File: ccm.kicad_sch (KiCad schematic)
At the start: 54 parts, among them J1 Conn_01x02_Socket, J10 Conn_01x02_Socket, J2 Conn_01x02_Socket, J3 Conn_01x02_Socket, J4 Conn_01x04_Socket, J5 Conn_01x02_Socket, J6 Conn_01x02_Socket, J7 Conn_01x02_Socket, J8 Conn_01x04_Socket, J9 Conn_01x02_Socket, Q1 IRLZ34N, U1 Teensy4.1, U2 PAM8302AAY, U3 SN65HVD230, U4 SN65HVD230, U5 LM1117DT-5.0

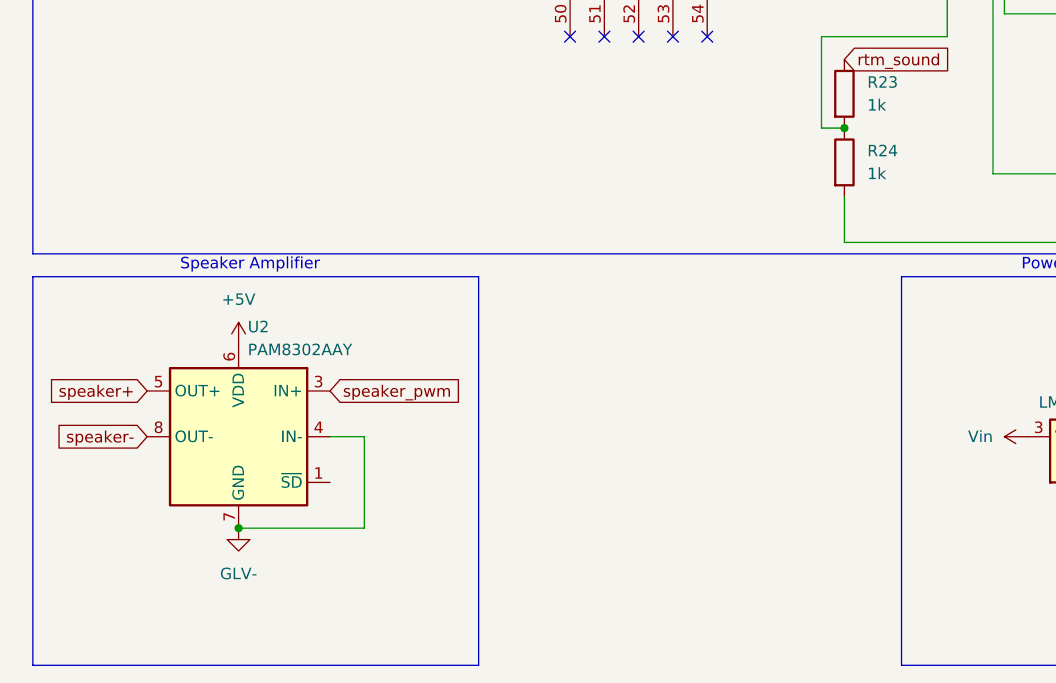
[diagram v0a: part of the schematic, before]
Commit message: added capacitors for amp
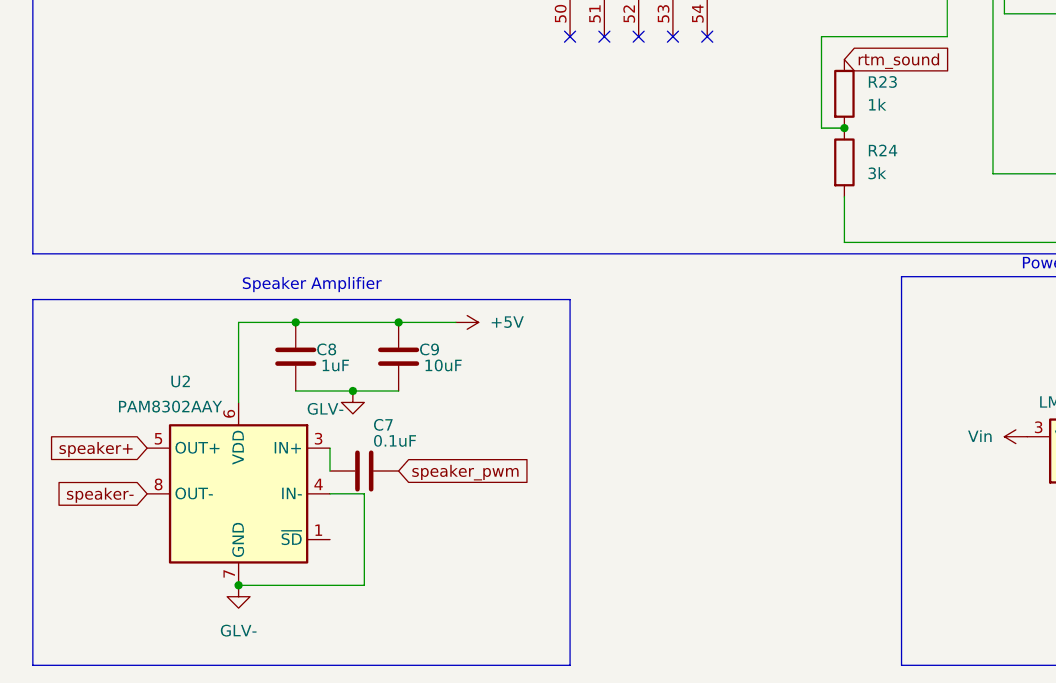
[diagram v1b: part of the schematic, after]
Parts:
- added C7: 0.1uF, Capacitor_SMD:C_0805_2012Metric, symbol Device:C
- added C8: 1uF, Capacitor_SMD:C_0805_2012Metric, symbol Device:C
- added C9: 10uF, Capacitor_SMD:C_0805_2012Metric, symbol Device:C
- R24: value 1k -> 3k
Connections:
- net +5V: now also C8.1, C9.1
- net GLV-: now also C8.2, C9.2
- net speaker_pwm: now also C7.2; no longer U2.3 (IN+)
- new net: C7.1, U2.3 (IN+)
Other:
- moved on the sheet: U2

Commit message: updated to revision schematic
tbd i/o connectors
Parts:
- added D1, D2, D3, D4: 1N5819, Diode_THT:D_DO-41_SOD81_P10.16mm_Horizontal, symbol Diode:1N5819
- added J11, J12, J15, J16: Conn_01x02_Socket, Connector_Molex:Molex_Mini-Fit_Jr_5566-02A2_2x01_P4.20mm_Vertical, symbol Connector:Conn_01x02_Socket
- added J13, J14: Conn_01x04_Socket, Connector_Molex:Molex_Mini-Fit_Jr_5566-04A2_2x02_P4.20mm_Vertical, symbol Connector:Conn_01x04_Socket
- added Q2, Q3, Q4, Q5: IRLZ34N, Package_TO_SOT_THT:TO-220-3_Vertical, symbol Transistor_FET:IRLZ34N
- added R33, R36, R38, R40: 220, symbol Device:R_US
- added R34, R35, R37, R39: 10k, symbol Device:R_US
- added R41, R42, R43, R44: 10k, Resistor_SMD:R_0805_2012Metric, symbol Device:R
- added TH1, TH2, TH3, TH4: Thermistor, symbol Device:Thermistor
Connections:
- net +3.3V: now also R41.2, R42.2, R43.2, R44.2
- net GLV-: now also Q2.3 (S), Q3.3 (S), Q4.3 (S), Q5.3 (S), R34.2, R35.2, R37.2, R39.2, TH1.2, TH2.2, TH3.2, TH4.2
- net lin_pot_1: now also J13.4 (Pin_4), J14.4 (Pin_4)
- net lin_pot_2: now also J13.3 (Pin_3), J14.3 (Pin_3)
- net lin_pot_3: now also J13.2 (Pin_2), J14.2 (Pin_2)
- net lin_pot_4: now also J13.1 (Pin_1), J14.1 (Pin_1)
- net at U1.18 (26_A12_MOSI1): now also R33.2, R34.1
- net at U1.19 (27_A13_SCK1): now also R35.1, R36.2
- net at U1.20 (28_RX7): now also R37.1, R38.2
- net at U1.21 (29_TX7): now also R39.1, R40.2
- net gpio2: now reaches U1.25 (33_MCLK2)
- net gpio3: now reaches U1.26 (34_RX8)
- net flowsensor4: now reaches U1.27 (35_TX8)
- net flowsensor3: now reaches U1.28 (36_CS)
- net flowsensor2: now reaches U1.29 (37_CS)
- net flowsensor1: now reaches U1.30 (38_CS1_IN1)
- net at U1.31 (39_MISO1_OUT1A): now also R44.1, TH4.1
- net at U1.32 (40_A16): now also R43.1, TH3.1
- net at U1.33 (41_A17): now also R42.1, TH2.1
- net at U1.36 (14_A0_TX3_SPDIF_OUT): now also R41.1, TH1.1
- new net: Q2.1 (G), R33.1
- new net: Q5.1 (G), R40.1
- new net: Q3.1 (G), R36.1
- new net: Q4.1 (G), R38.1
- new net +24V: D1.1 (K), D2.1 (K), D3.1 (K), D4.1 (K)
- new net Fan1-: D3.2 (A), Q4.2 (D)
- new net Fan2-: D4.2 (A), Q5.2 (D)
- new net Pump1-: D1.2 (A), Q2.2 (D)
- new net Pump2-: D2.2 (A), Q3.2 (D)
- no-connect marks 45 -> 29
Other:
- moved on the sheet: C1, C2, C3, C4, C5, C6, C7, C8, C9, J1, J10, J2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

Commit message: add i/o connectors
tbd pcb revision
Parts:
- added J17, J18: Conn_01x02_Socket, Connector_Molex:Molex_Mini-Fit_Jr_5566-02A2_2x01_P4.20mm_Vertical, symbol Connector:Conn_01x02_Socket
- added J19: Conn_01x04_Socket, Connector_Molex:Molex_Mini-Fit_Jr_5566-04A2_2x02_P4.20mm_Vertical, symbol Connector:Conn_01x04_Socket
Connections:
- net gpio3 is gone; now on net gpio2: U1.26 (34_RX8)
- net +24V: now also J11.1 (Pin_1), J12.1 (Pin_1), J15.1 (Pin_1), J16.1 (Pin_1)
- net Fan1-: now also J15.2 (Pin_2)
- net Fan2-: now also J16.2 (Pin_2)
- net GLV-: now also J17.2 (Pin_2), J18.2 (Pin_2)
- net Pump1-: now also J11.2 (Pin_2)
- net Pump2-: now also J12.2 (Pin_2)
- net flowsensor1: now also J13.4 (Pin_4)
- net flowsensor2: now also J13.3 (Pin_3)
- net flowsensor3: now also J13.2 (Pin_2)
- net flowsensor4: now also J13.1 (Pin_1)
- net gpio2: now also J18.1 (Pin_1); no longer U1.25 (33_MCLK2)
- net lin_pot_1: no longer J13.4 (Pin_4), J14.4 (Pin_4)
- net lin_pot_2: no longer J13.3 (Pin_3), J14.3 (Pin_3)
- net lin_pot_3: no longer J13.2 (Pin_2), J14.2 (Pin_2)
- net lin_pot_4: no longer J13.1 (Pin_1), J14.1 (Pin_1)
- new net gpio1: J17.1 (Pin_1), U1.25 (33_MCLK2)
- new net thermistor1+: J19.1 (Pin_1)
- new net thermistor1-: J14.1 (Pin_1)
- new net thermistor2+: J19.2 (Pin_2)
- new net thermistor2-: J14.2 (Pin_2)
- new net thermistor3+: J19.3 (Pin_3)
- new net thermistor3-: J14.3 (Pin_3)
- new net thermistor4+: J19.4 (Pin_4)
- new net thermistor4-: J14.4 (Pin_4)
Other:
- note added: "Extra GPIO"
- note added: "Flow Speed Sensors"
- note added: "Pump/Fan Output"
- note added: "Ready To Move Signal"
- note added: "Thermistor"
- note removed: "Board I/O"
- moved on the sheet: C7, C8, C9, J1, J10, J11, J12, J13, J14, J15, J16, J2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

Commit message: ccm schem complete
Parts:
- removed D1, D2, D3, D4: 1N5819, Diode_THT:D_DO-41_SOD81_P10.16mm_Horizontal, symbol Diode:1N5819
- removed J13, J14, J19: Conn_01x04_Socket, Connector_Molex:Molex_Mini-Fit_Jr_5566-04A2_2x02_P4.20mm_Vertical, symbol Connector:Conn_01x04_Socket
- added D1, D2, D3, D4: SS14, Diode_SMD:D_SMA, symbol Diode:SS14
- added J13, J14, J19, J20, J21, J22, J23, J24: Conn_01x02_Socket, Connector_Molex:Molex_Mini-Fit_Jr_5566-02A2_2x01_P4.20mm_Vertical, symbol Connector:Conn_01x02_Socket
- R33, R34, R35, R36, R37, R38, R39, R40: footprint (none) -> Resistor_SMD:R_0805_2012Metric
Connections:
- net +24V: now also D1.1 (K), D2.1 (K), D3.1 (K), D4.1 (K)
- net Fan1-: now also D3.2 (A)
- net Fan2-: now also D4.2 (A)
- net GLV-: now also J13.2 (Pin_2), J19.2 (Pin_2), J20.2 (Pin_2), J21.2 (Pin_2), J22.2 (Pin_2), J23.2 (Pin_2)
- net Pump1-: now also D1.2 (A)
- net Pump2-: now also D2.2 (A)
- net thermistor1+: now also R41.1, TH1.1, U1.36 (14_A0_TX3_SPDIF_OUT), J21.1 (Pin_1)
- net thermistor2+: now also R42.1, TH2.1, U1.33 (41_A17), J19.1 (Pin_1)
- net thermistor3+: now also R43.1, TH3.1, U1.32 (40_A16), J22.1 (Pin_1)
- net thermistor4+: now also J23.1 (Pin_1)
- net Fan2_PWM: now reaches U1.10 (8_TX2_IN1)
- net Fan2_PWM: now also J24.2 (Pin_2)
- net Pump1_PWM: now reaches U1.7 (5_IN2)
- net Pump1_PWM: now also J14.1 (Pin_1)
- net Pump2_PWM: now reaches U1.8 (6_OUT1D)
- net Pump2_PWM: now also J14.2 (Pin_2)
- net Fan1_PWM: now reaches U1.9 (7_RX2_OUT1A)
- net Fan1_PWM: now also J24.1 (Pin_1)
- net flowsensor1: no longer names the net of U1.30 (38_CS1_IN1)
- net flowsensor2: no longer names the net of U1.29 (37_CS)
- net flowsensor3 renamed gpio4
- net gpio4: now also J20.1 (Pin_1)
- net flowsensor4 renamed gpio3
- net gpio3: now also J13.1 (Pin_1)
- no-connect marks 29 -> 25
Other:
- note added: "Extra GPIO Pins"
- note added: "Pump/Fan PWM OUT"
- note removed: "Extra GPIO"
- note removed: "Flow Speed Sensors"
- moved on the sheet: J1, J10, J11, J12, J15, J16, J17, J18, J2, J3, J4, J5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

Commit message: layout v1
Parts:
- removed J14: Conn_01x02_Socket, Connector_Molex:Molex_Mini-Fit_Jr_5566-02A2_2x01_P4.20mm_Vertical, symbol Connector:Conn_01x02_Socket
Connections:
- net GLV-: no longer J19.2 (Pin_2), J21.2 (Pin_2), J22.2 (Pin_2), J23.2 (Pin_2)
- net Pump1_PWM: no longer names the net of U1.7 (5_IN2)
- net Pump2_PWM: no longer names the net of U1.8 (6_OUT1D)
- new net thermistor1-: J21.2 (Pin_2)
- new net thermistor2-: J19.2 (Pin_2)
- new net thermistor3-: J22.2 (Pin_2)
- new net thermistor4-: J23.2 (Pin_2)
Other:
- note added: "Fan PWM OUT"
- note added: "Ready To Move Signal (Redundant)"
- note removed: "Pump/Fan PWM OUT"
- note removed: "Ready To Move Signal"
- moved on the sheet: D1, D2, D3, D4, J24

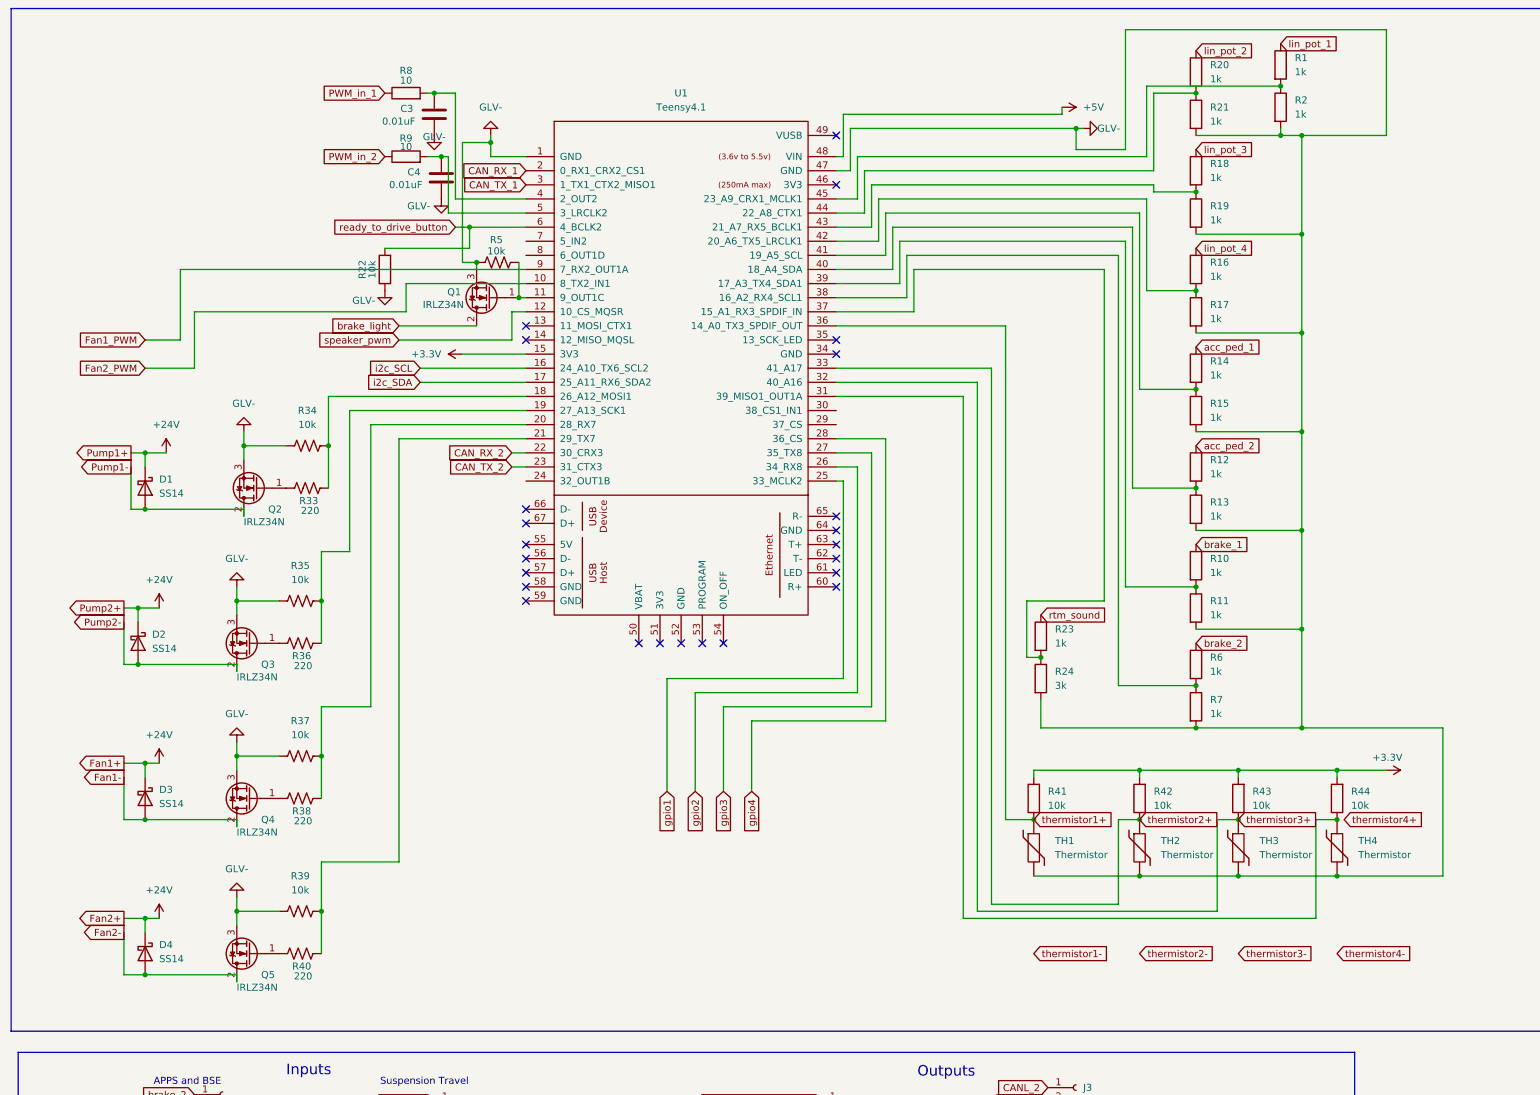
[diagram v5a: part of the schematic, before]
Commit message: add npn transistor level shifter for fan pwm
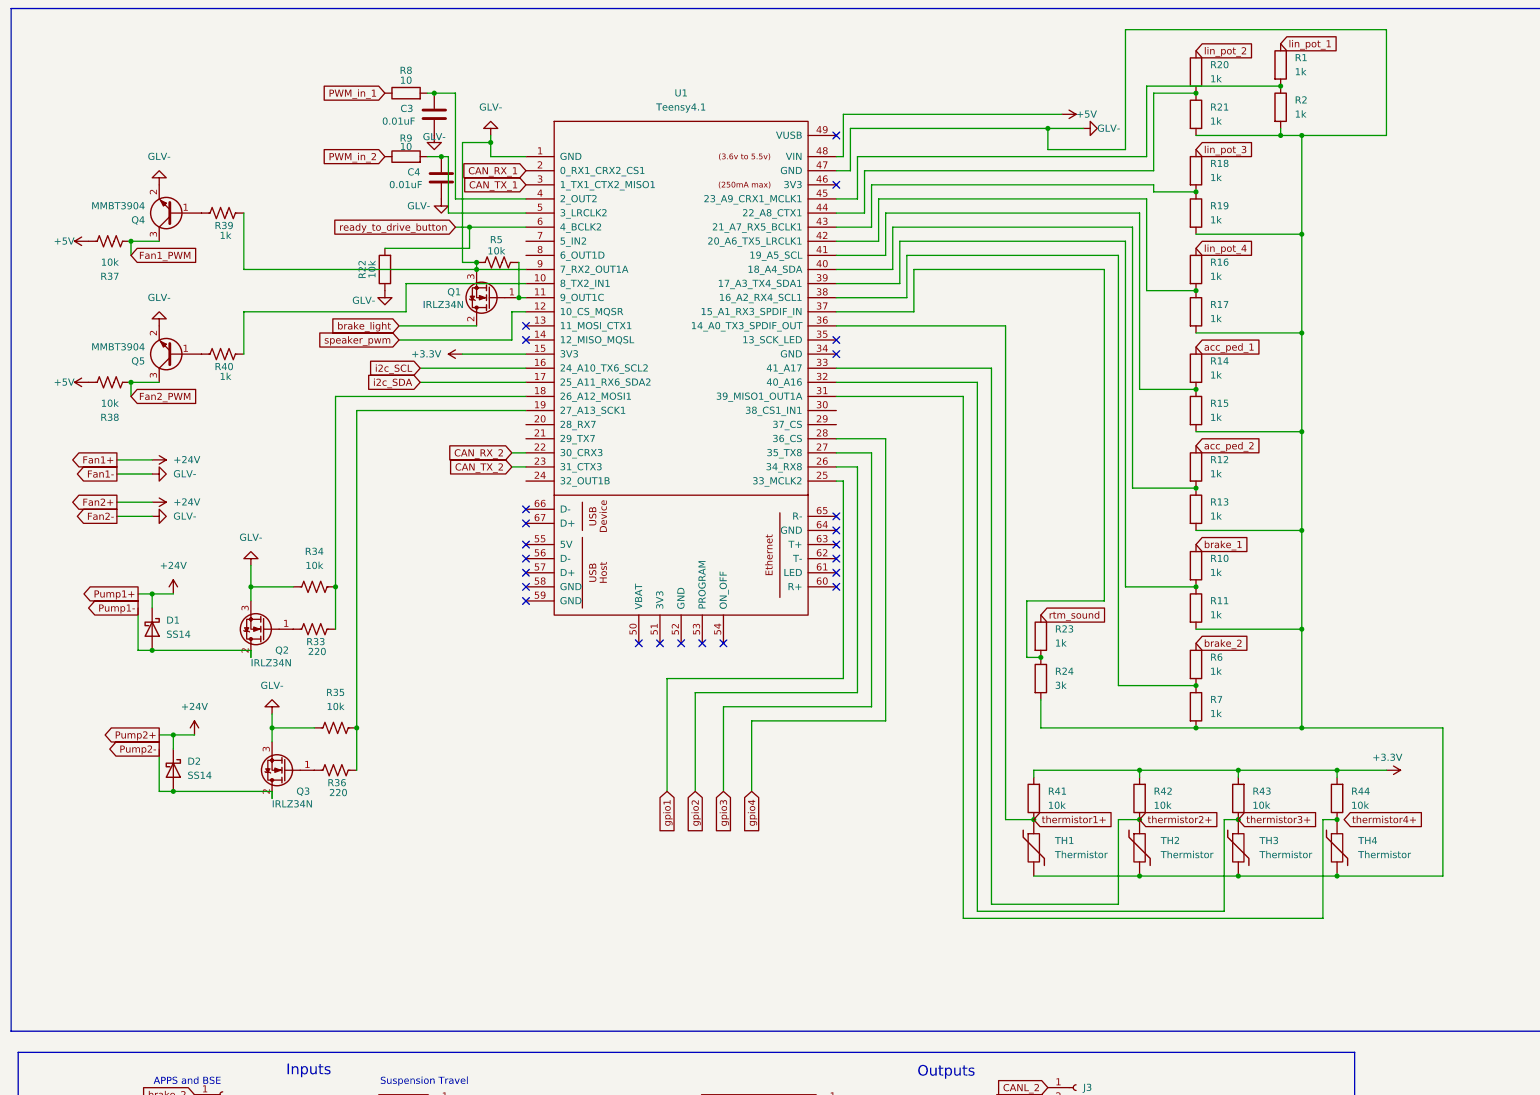
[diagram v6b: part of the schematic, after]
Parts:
- removed D3, D4: SS14, Diode_SMD:D_SMA, symbol Diode:SS14
- removed Q4, Q5: IRLZ34N, Package_TO_SOT_THT:TO-220-3_Vertical, symbol Transistor_FET:IRLZ34N
- added Q4, Q5: MMBT3904, Package_TO_SOT_SMD:SOT-23, symbol Transistor_BJT:MMBT3904
- R38: value 220 -> 10k
- R39: value 10k -> 1k
- R40: value 220 -> 1k
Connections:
- net Fan1- is gone; now on net GLV-: J15.2 (Pin_2)
- net Fan2- is gone; now on net GLV-: J16.2 (Pin_2)
- net +5V: now also R37.1, R38.1
- net Fan1_PWM: now also R37.2, Q4.3 (C); no longer U1.9 (7_RX2_OUT1A)
- net Fan2_PWM: now also R38.2, Q5.3 (C); no longer U1.10 (8_TX2_IN1)
- net GLV-: now also U1.9 (7_RX2_OUT1A), Q4.2 (E), Q5.2 (E); no longer R37.2
- net at R40.1: now also Q5.1 (B)
- new net: R40.2, U1.10 (8_TX2_IN1)
- new net: Q4.1 (B), R39.1
- now unconnected: U1.20 (28_RX7), U1.21 (29_TX7)
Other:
- moved on the sheet: D1, D2, Q2, Q3, R33, R34, R35, R36
